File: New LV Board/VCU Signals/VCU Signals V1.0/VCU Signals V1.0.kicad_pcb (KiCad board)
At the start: 2 copper layers, 46 x 51.3 mm, 15 parts, among them J1 B12B-PH-K-S:JST_B12B-PH-K-S, P1 PH1-20-UA, P2 PH1-20-UA, U1 IRLML2060TRPBF, U2 IRLML2060TRPBF, U3 IRLML2060TRPBF

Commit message: updated VCU signals with substitute mosfets
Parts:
- R2, R4, R6: value 150 -> 150R
- U1, U2, U3: value IRLML2060TRPBF -> IRLU014PBF; footprint Motorsports:DPAK-3_6P35X6P73_ONS -> Package_TO_SOT_THT:TO-251-3_Vertical
- moved P1 1.80 mm to (125.7, 125.7)
- moved R3 1.80 mm to (95.6, 110.5)
- moved R6 1.80 mm to (95.5, 124.3)
- moved U3 1.80 mm to (109.8, 120.5)
- moved D1 1.80 mm to (109.8, 108.5)
- moved D2 1.80 mm to (109.8, 116.6)
- moved D3 1.80 mm to (109.8, 124.7)
- moved J1 1.80 mm to (118.4, 124.9)
- moved P2 1.80 mm to (82.5, 125.7)
- moved R1 1.80 mm to (95.6, 101.3)
- moved R2 1.80 mm to (95.6, 105.9)
- moved R4 1.80 mm to (95.6, 115.1)
- moved R5 1.80 mm to (95.6, 119.6)
- moved U1 1.80 mm to (109.8, 104.4)
- moved U2 1.80 mm to (109.9, 112.5)

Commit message: Jack bro...
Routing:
- net Net-(D2-A): track 18.5 -> 21.9 mm
- net Net-(U1-G): track 24.2 -> 25.1 mm
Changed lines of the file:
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@@
 		(tags "TO-251-3 Vertical RM 2.29mm IPAK")
 		(property "Reference" "U3"
-			(at 2.29 -2.22 0)
+			(at -2.0916 -1.397 0)
 			(layer "F.SilkS")
 			(effects
@@
 		)
 		(property "Value" "IRLU014PBF"
-			(at 2.29 1.98 0)
+			(at 2.3534 2.032 0)
 			(layer "F.Fab")
 			(effects
@@
 		(tags "LED")
 		(property "Reference" "D2"
-			(at -1.15 -1.524 0)
+			(at -2.0916 0 0)
 			(layer "F.SilkS")
 			(effects
@@
 		)
 		(property "Value" "LED (Test)"
-			(at 1.27 1.5 180)
+			(at -3.3616 0.762 180)
 			(layer "F.Fab")
 			(effects
@@
 	)
 	(segment
-		(start 108.6381 113.050744)
-		(end 108.6381 111.993256)
+		(start 107.95 110.998)
+		(end 111.76 110.998)
 		(width 0.5)
 		(layer "B.Cu")
@@
 	)
 	(segment
-		(start 108.6381 111.993256)
-		(end 109.385856 111.2455)
+		(start 111.76 112.0774)
+		(end 112.2046 112.522)
 		(width 0.5)
 		(layer "B.Cu")
@@
 	)
 	(segment
-		(start 110.9241 111.2455)
-		(end 112.2006 112.522)
+		(start 109.22 114.554)
+		(end 107.95 113.284)
 		(width 0.5)
 		(layer "B.Cu")
@@
 	)
 	(segment
-		(start 109.385856 111.2455)
-		(end 110.9241 111.2455)
+		(start 112.3276 116.586)
+		(end 112.3276 115.8836)
+		(width 0.5)
+		(layer "B.Cu")
+		(net 4)
+	)
+	(segment
+		(start 110.998 114.554)
+		(end 109.22 114.554)
 		(width 0.5)
 		(layer "B.Cu")
@@
 	)
 	(segment
-		(start 112.3276 116.586)
-		(end 110.8036 115.062)
+		(start 107.95 113.284)
+		(end 107.95 110.998)
 		(width 0.5)
 		(layer "B.Cu")
@@
 	)
 	(segment
-		(start 110.8036 115.062)
-		(end 110.649356 115.062)
+		(start 112.3276 115.8836)
+		(end 110.998 114.554)
 		(width 0.5)
 		(layer "B.Cu")
@@
 	)
 	(segment
-		(start 110.649356 115.062)
-		(end 108.6381 113.050744)
+		(start 111.76 110.998)
+		(end 111.76 112.0774)
 		(width 0.5)
 		(layer "B.Cu")
@@
 	)
 	(segment
-		(start 114.888344 103.1175)
-		(end 111.0641 103.1175)
+		(start 116.207 103.507)
+		(end 116.207 112.628)
 		(width 0.5)
 		(layer "F.Cu")
@@
 	)
 	(segment
-		(start 116.207 104.436156)
-		(end 114.888344 103.1175)
+		(start 115.316 102.616)
+		(end 116.207 103.507)
 		(width 0.5)
 		(layer "F.Cu")
@@
 	)
 	(segment
-		(start 111.0641 103.1175)
-		(end 109.7876 104.394)
+		(start 105.7236 101.346)
+		(end 108.7716 104.394)
 		(width 0.5)
 		(layer "F.Cu")
@@
 	)
 	(segment
-		(start 105.7236 101.346)
-		(end 108.7716 104.394)
+		(start 111.5656 102.616)
+		(end 115.316 102.616)
 		(width 0.5)
 		(layer "F.Cu")
@@
 	)
 	(segment
-		(start 118.449 114.87)
-		(end 116.207 112.628)
+		(start 116.207 112.628)
+		(end 118.449 114.87)
 		(width 0.5)
 		(layer "F.Cu")
@@
 	)
 	(segment
-		(start 116.207 112.628)
-		(end 116.207 104.436156)
+		(start 109.7876 104.394)
+		(end 111.5656 102.616)
 		(width 0.5)
 		(layer "F.Cu")

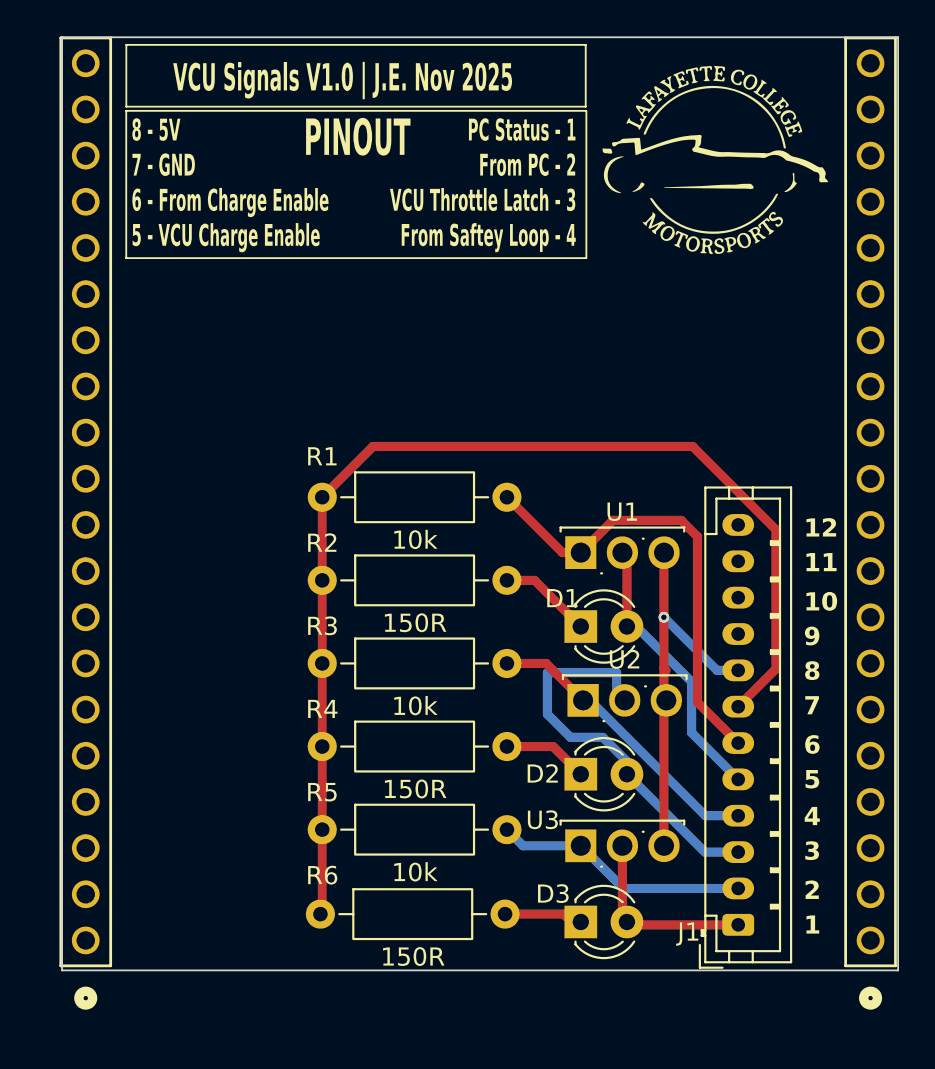
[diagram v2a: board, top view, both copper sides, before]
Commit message: AMS & IMD fixing some connections
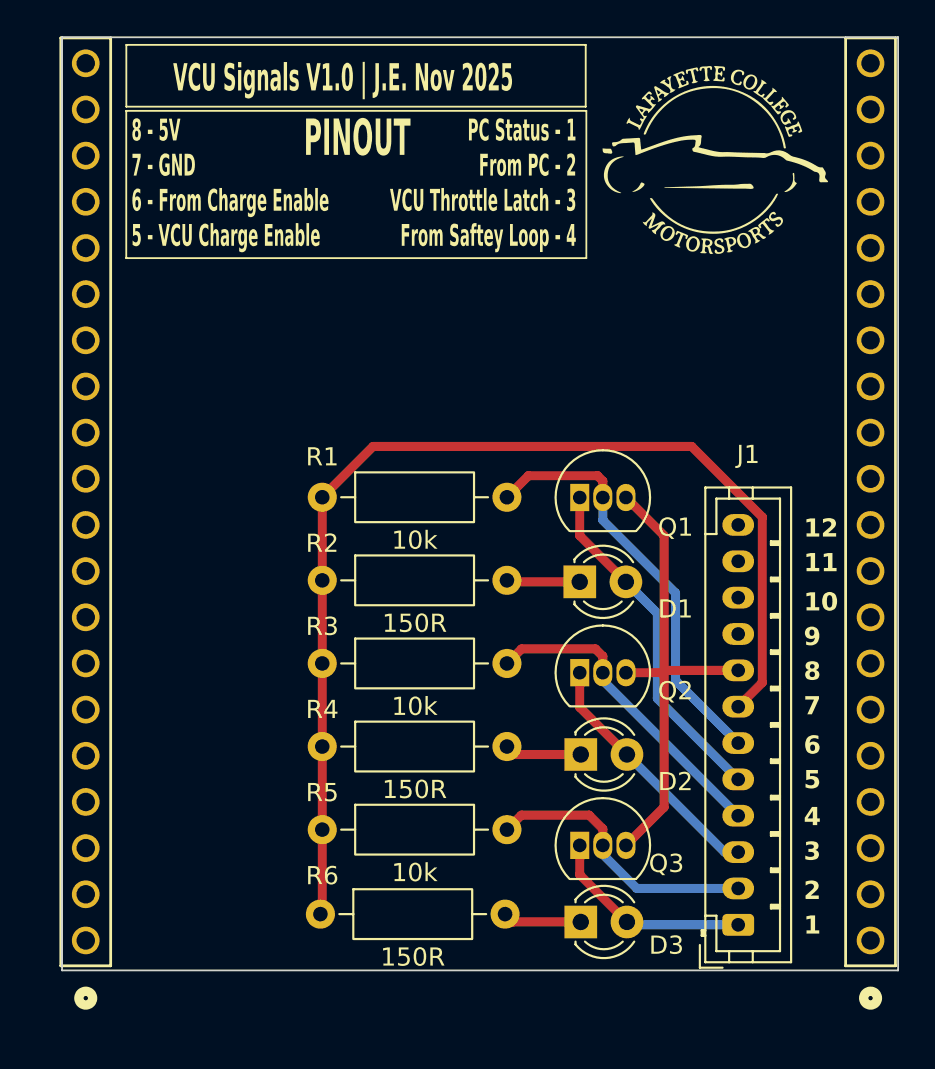
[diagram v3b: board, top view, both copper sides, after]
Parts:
- removed U1, U2, U3: IRLU014PBF, Package_TO_SOT_THT:TO-251-3_Vertical
- added Q1: ZVN2110A, Package_TO_SOT_THT:TO-92_Inline, F.Cu at (109.7, 101.4)
- added Q2: ZVN2110A, Package_TO_SOT_THT:TO-92_Inline, F.Cu at (109.7, 111.0)
- added Q3: ZVN2110A, Package_TO_SOT_THT:TO-92_Inline, F.Cu at (109.7, 120.5)
- moved D1 2.46 mm to (109.7, 106.0)
- moved D2 1.09 mm to (109.8, 115.5)
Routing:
- net Net-(D2-A): track 21.9 -> 13.9 mm
- net Net-(Q1-D): track 21.6 -> 27.1 mm, vias 1 -> 0
- net Net-(D1-A): track 15.4 -> 19.1 mm
- net Net-(Q1-G): track 25.1 -> 23.4 mm
- net Net-(Q3-G): track 14.1 -> 15.6 mm
- net Net-(Q2-G): track 16.2 -> 17.6 mm
- net Net-(D1-K): track 5.12 -> 4.04 mm
- net Net-(D3-A): track 10.5 -> 11.5 mm
- net Net-(J1-Pad7): track 61.6 -> 60.9 mm
